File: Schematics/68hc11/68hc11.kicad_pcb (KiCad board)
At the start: 2 copper layers, 268.6 x 177.2 mm, 25 parts, among them J1 DB9_Female, J2 Screw_Terminal_01x10, J3 Screw_Terminal_01x10, J4 Screw_Terminal_01x10, J5 Screw_Terminal_01x10, SW1 Reset, U1 MC68HC11A1CC-PLLC, U10 MCP100-270D, U2 MC68B21, U3 74HC373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

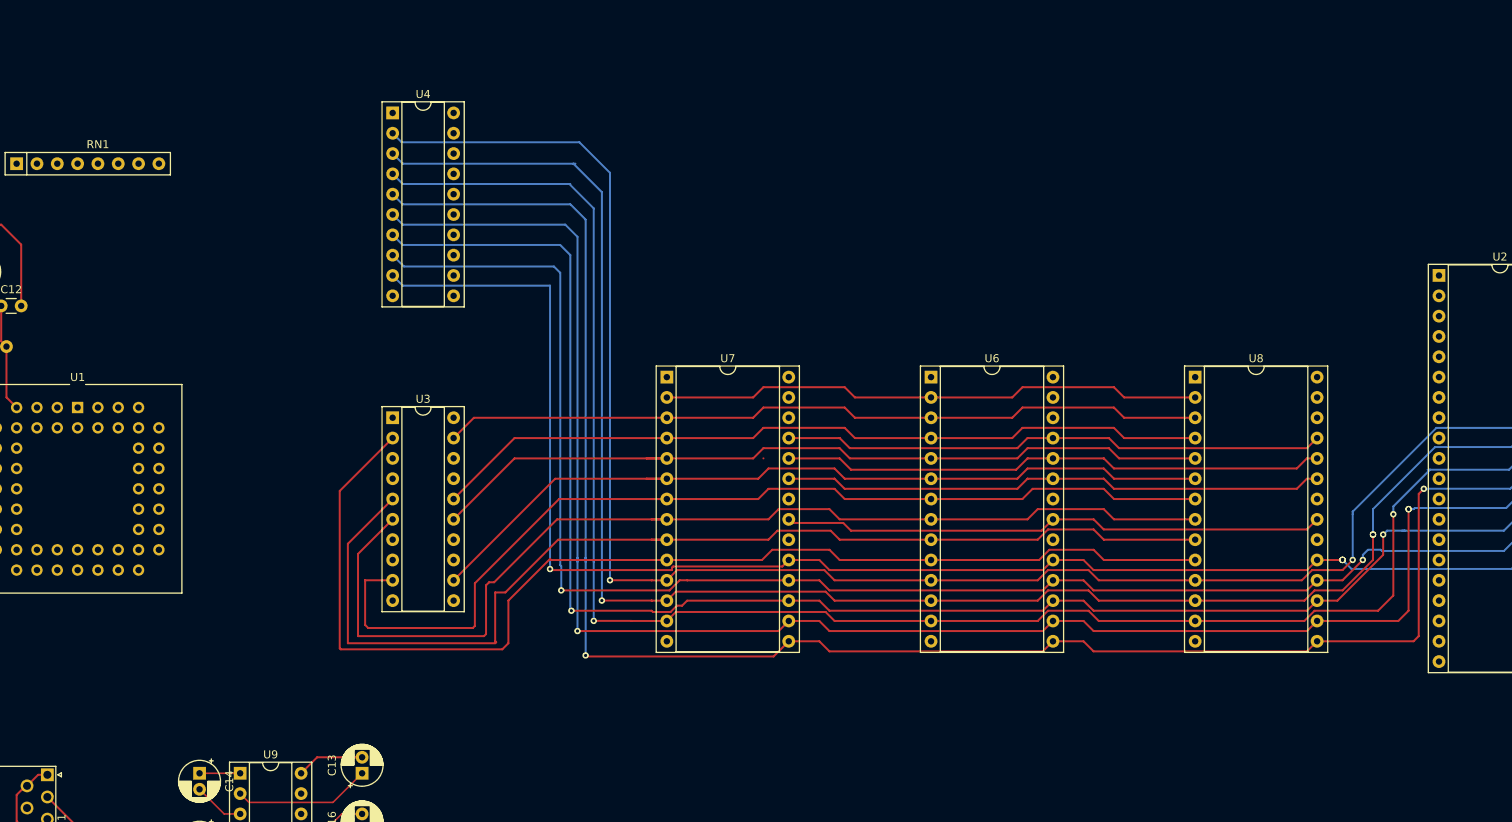
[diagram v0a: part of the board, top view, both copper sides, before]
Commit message: Added bypass caps to chips
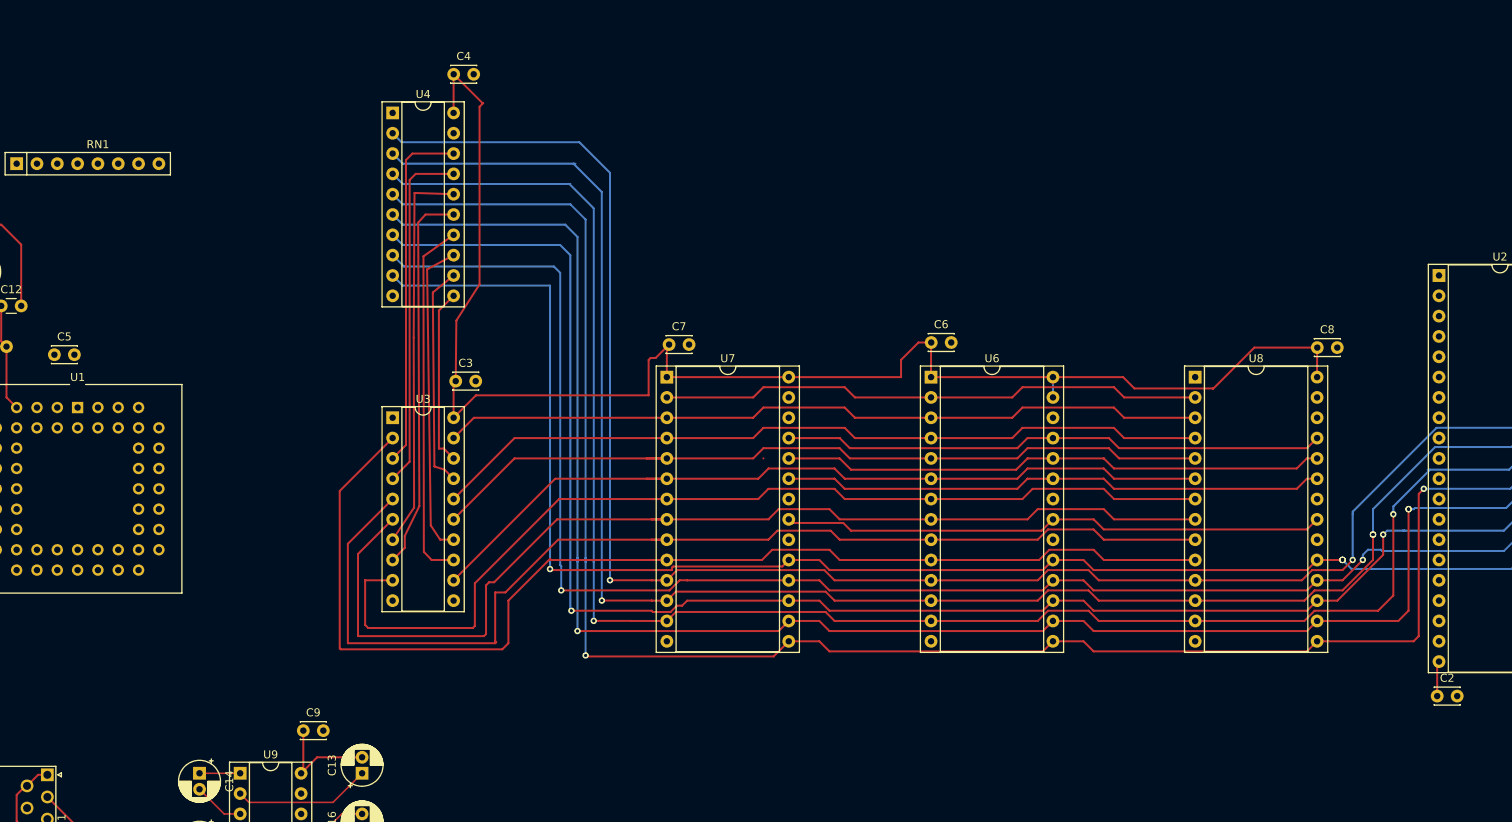
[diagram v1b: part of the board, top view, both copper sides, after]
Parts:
- added C2: 0.1uF, Capacitor_THT:C_Disc_D3.0mm_W2.0mm_P2.50mm, F.Cu at (213.1, 137.7)
- added C3: 0.1uF, Capacitor_THT:C_Disc_D3.0mm_W2.0mm_P2.50mm, F.Cu at (90.4, 98.3)
- added C4: 0.1uF, Capacitor_THT:C_Disc_D3.0mm_W2.0mm_P2.50mm, F.Cu at (90.2, 59.9)
- added C5: 0.1uF, Capacitor_THT:C_Disc_D3.0mm_W2.0mm_P2.50mm, F.Cu at (40.3, 95.0)
- added C6: 0.1uF, Capacitor_THT:C_Disc_D3.0mm_W2.0mm_P2.50mm, F.Cu at (149.9, 93.5)
- added C7: 0.1uF, Capacitor_THT:C_Disc_D3.0mm_W2.0mm_P2.50mm, F.Cu at (117.1, 93.7)
- added C8: 0.1uF, Capacitor_THT:C_Disc_D3.0mm_W2.0mm_P2.50mm, F.Cu at (198.1, 94.1)
- added C9: 0.1uF, Capacitor_THT:C_Disc_D3.0mm_W2.0mm_P2.50mm, F.Cu at (71.4, 142.0)
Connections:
- J2 pad 1: unconnected-(J2-Pad1) -> GND
- J2 pad 3: unconnected-(J2-Pad3) -> /PA0
- J2 pad 4: unconnected-(J2-Pad4) -> /PA1
- J2 pad 5: unconnected-(J2-Pad5) -> /PA2
- J2 pad 6: unconnected-(J2-Pad6) -> /PA3
- J2 pad 7: unconnected-(J2-Pad7) -> /PA4
- J2 pad 8: unconnected-(J2-Pad8) -> /PA5
- J2 pad 9: unconnected-(J2-Pad9) -> /PA6
- J3 pad 1: unconnected-(J3-Pad1) -> +5V
- J3 pad 2: unconnected-(J3-Pad2) -> /PE0
- J3 pad 3: unconnected-(J3-Pad3) -> /PE1
- J3 pad 4: unconnected-(J3-Pad4) -> /PE2
- J3 pad 5: unconnected-(J3-Pad5) -> /PE3
- J3 pad 6: unconnected-(J3-Pad6) -> /PE4
- J3 pad 7: unconnected-(J3-Pad7) -> /PE5
- J3 pad 8: unconnected-(J3-Pad8) -> /PE6
- J3 pad 9: unconnected-(J3-Pad9) -> /PE7
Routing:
- net +5V: track 8.45 -> 205.9 mm
- net /AD2: track 0.00 -> 49.0 mm
- net /AD3: track 0.00 -> 48.1 mm
- net /AD4: track 0.00 -> 45.7 mm
- net /AD0: track 0.00 -> 44.3 mm
- net /AD1: track 0.14 -> 44.2 mm
- net /AD5: track 0.00 -> 39.6 mm
- net /AD6: track 0.00 -> 28.0 mm
- net /AD7: track 0.00 -> 22.2 mm

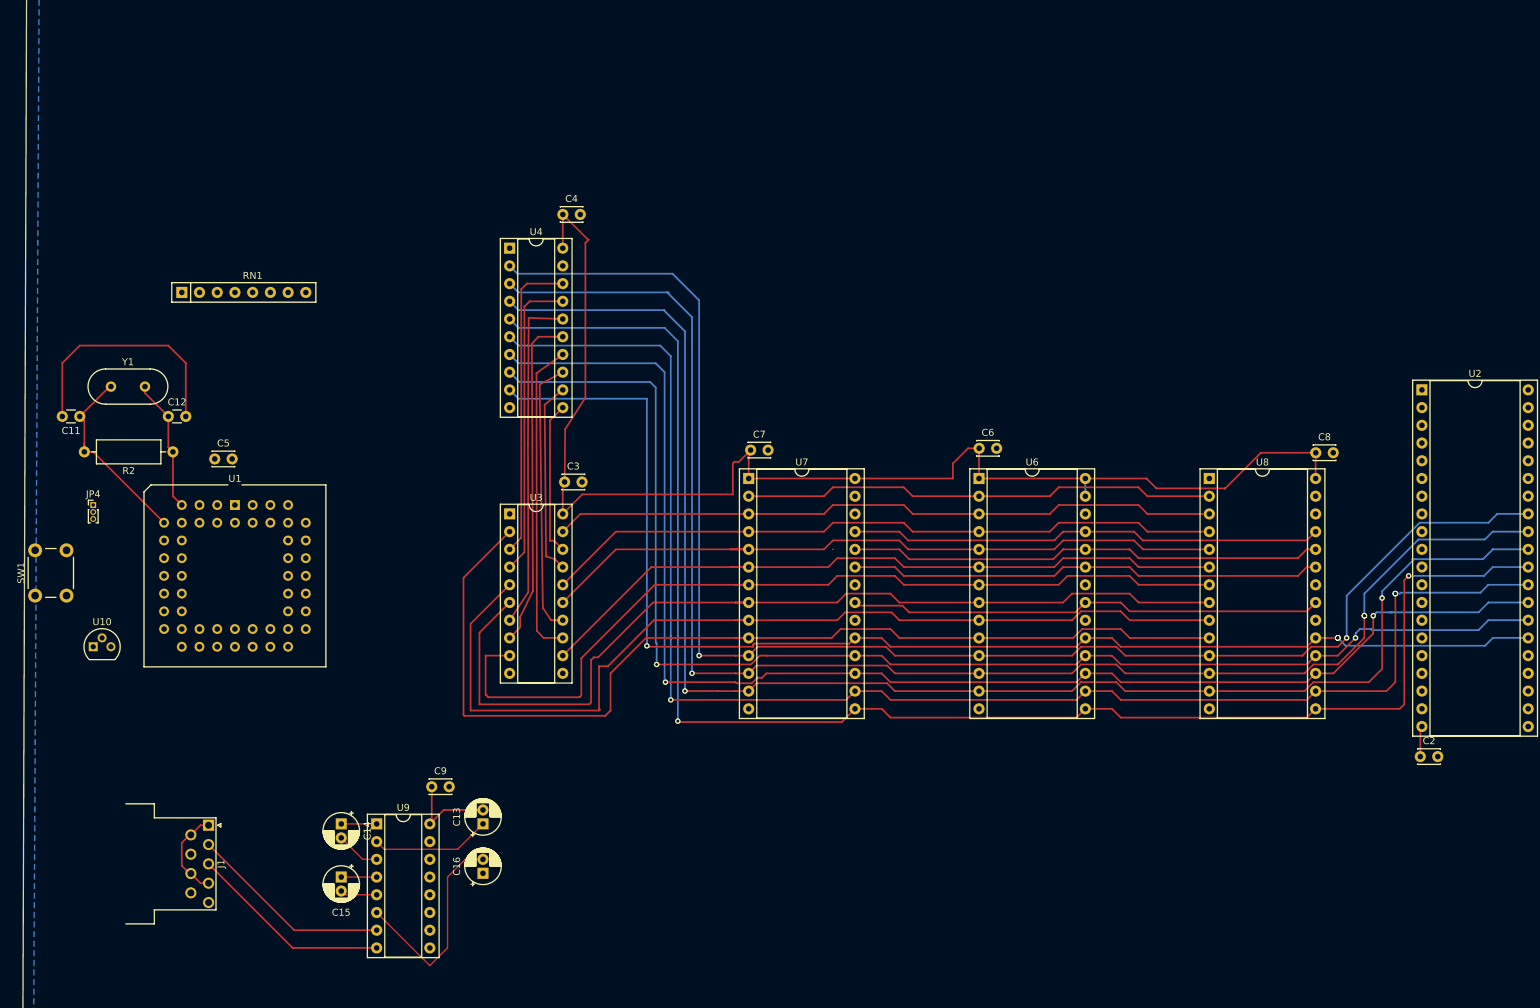
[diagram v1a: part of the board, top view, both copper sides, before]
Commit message: Cleaned up AD traces and all warnings
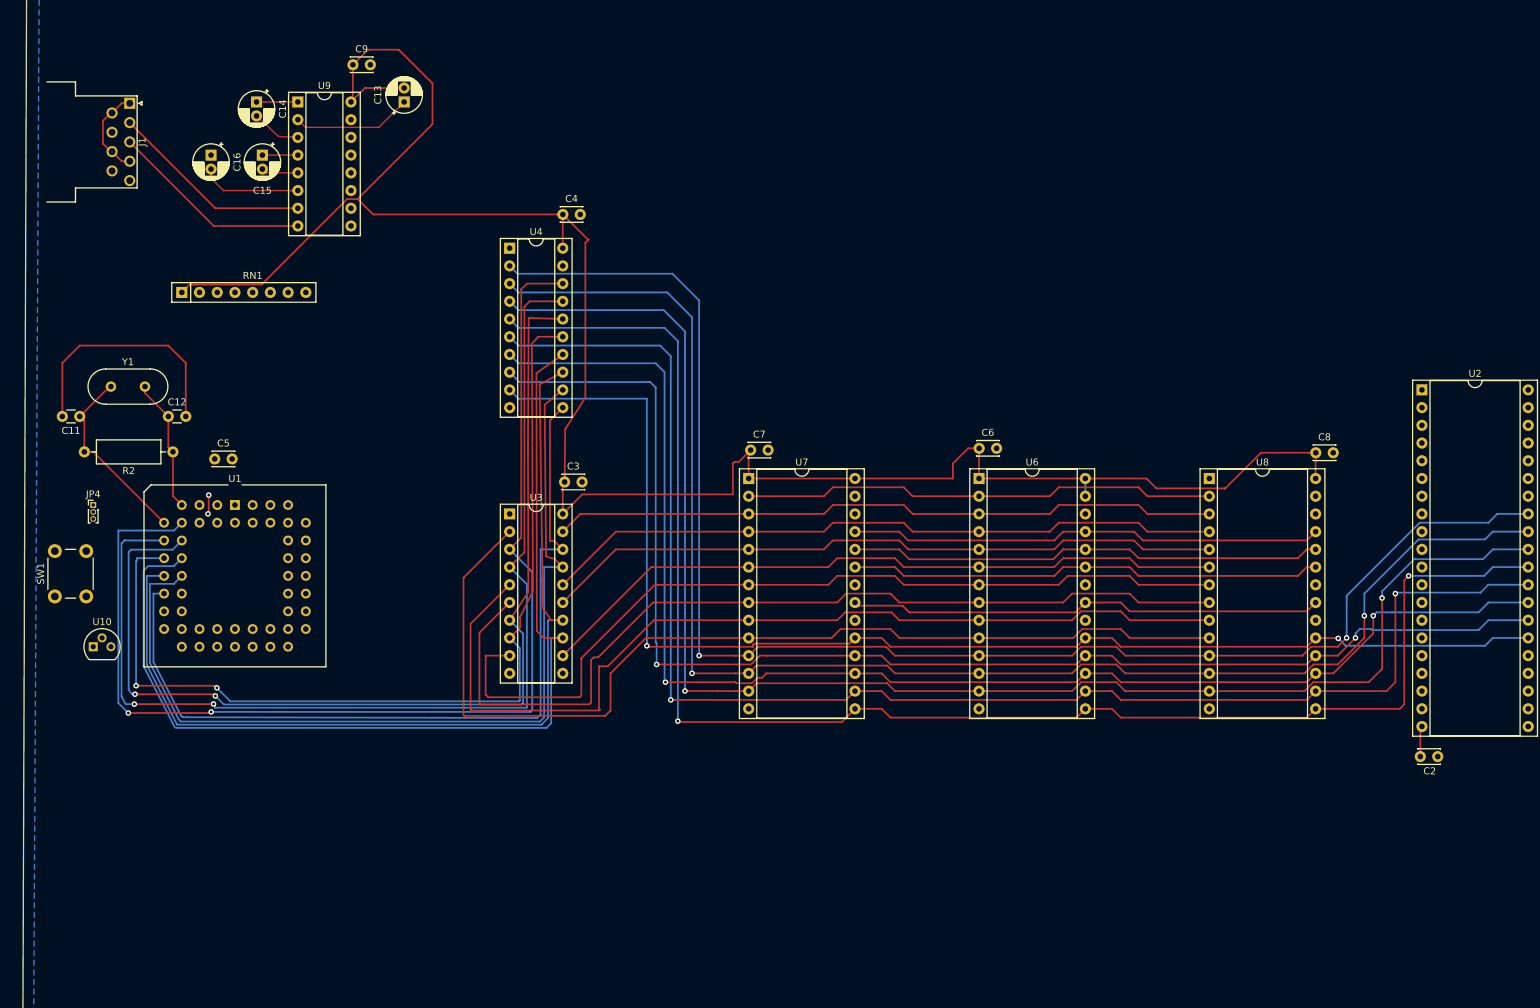
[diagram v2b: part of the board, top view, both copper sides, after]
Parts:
- moved C16 110.1 mm to (39.8, 51.4), turned to -90 degrees
- moved C14 104.2 mm to (46.3, 43.8)
- moved J1 104.1 mm to (28.1, 44.0)
- moved C13 104.1 mm to (67.4, 43.8)
- moved C15 104.1 mm to (47.1, 51.4)
- moved C9 104.1 mm to (60.1, 38.5)
- moved U9 104.1 mm to (52.2, 43.8)
- moved SW1 2.83 mm to (17.4, 114.7)
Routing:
- net /AD0: track 44.3 -> 163.1 mm, vias 0 -> 2
- net /AD1: track 44.2 -> 152.6 mm, vias 0 -> 2
- net /AD6: track 28.0 -> 130.5 mm
- net /AD7: track 22.2 -> 120.9 mm
- net /AD2: track 49.0 -> 147.3 mm, vias 0 -> 2
- net /AD4: track 45.7 -> 143.4 mm
- net +5V: track 205.9 -> 300.3 mm
- net /AD5: track 39.6 -> 133.8 mm
- net /AD3: track 48.1 -> 135.9 mm, vias 0 -> 2
- net /VS-: track 30.7 -> 14.5 mm
- net GND: track 35.1 -> 37.8 mm, vias 0 -> 2
- net /A5: track 100.5 -> 98.0 mm
- net /A4: track 102.6 -> 100.1 mm
- net /A1: track 139.3 -> 137.4 mm
- net /A3: track 126.8 -> 124.9 mm
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
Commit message: Added power jack
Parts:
- added C1: 100uF, Capacitor_THT:CP_Radial_D5.0mm_P2.00mm, F.Cu at (50.8, 36.3)
- added D1: LED, LED_THT:LED_D5.0mm, F.Cu at (67.5, 32.4)
- added J1: DC 5 Volts, Connector_BarrelJack:BarrelJack_CUI_PJ-063AH_Horizontal_CircularHoles, F.Cu at (27.1, 35.7)
- added R1: 330, Resistor_THT:R_Axial_DIN0204_L3.6mm_D1.6mm_P7.62mm_Horizontal, F.Cu at (60.9, 32.4)
- moved J2 8.02 mm to (28.4, 52.0)
- moved U10 1.55 mm to (23.3, 120.4), turned to -90 degrees
- moved SW1 1.07 mm to (18.4, 114.7)
- renumbered J1 to J2, J2 to J3, J3 to J4, J4 to J5, J5 to J6
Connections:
- net +5V renamed VCC
- U1 pad 4: GND -> /AS
- U3 pad 11: GND -> /AS
- U4 pad 19: GND -> /AS
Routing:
- net VCC: track 300.3 -> 456.0 mm
- net /PE0: track 0.00 -> 30.7 mm
- net /*RESET: track 0.00 -> 22.8 mm
- net /R2IN: track 29.1 -> 24.4 mm
- net /T2OUT: track 29.2 -> 24.6 mm
- net Net-(D1-Pad2): track 0.00 -> 4.07 mm
